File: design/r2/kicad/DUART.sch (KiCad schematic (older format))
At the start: 15 parts, among them IC1 XR68C681CJTR-F, J2 UART_A, J3 UART_B, J4 Conn_01x06, Q1 Crystal

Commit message: Complete schematic capture for r2
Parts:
- removed C11, C12: 100nF, rosco_m68k:C2.5-3, symbol Device:C
- removed C13, C14: 220uF, Capacitor_THT:CP_Radial_D6.3mm_P2.50mm, symbol Device:CP
- removed JP1-5: Conn_02x05_Odd_Even, Connector_PinHeader_2.54mm:PinHeader_2x05_P2.54mm_Vertical, symbol Connector_Generic:Conn_02x05_Odd_Even
- added JP1, JP2: Jumper, Connector_PinHeader_2.54mm:PinHeader_1x02_P2.54mm_Vertical, symbol Device:Jumper
- renumbered C3 to C1, C5 to C2, C8 to C28, C9 to C29, C10 to C30, IC1 to IC4, J2 to J1, J3 to J2
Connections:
- net labels added: IPL2, RW
- net labels removed: IPL3, RnW
- wire segments 50 -> 32
- no-connect marks 6 -> 4
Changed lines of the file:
@@
 $Descr A4 11693 8268
 encoding utf-8
-Sheet 5 5
+Sheet 4 7
 Title "ROSCO_M68K GENERAL PURPOSE MC68010 COMPUTER"
 Date "2021-10-08"
@@
 $EndComp
 $Comp
-L Device:C C3
+L Device:C C1
 U 1 1 5EDD83D0
 P 7550 3850
-F 0 "C3" H 7665 3896 50  0000 L CNN
+F 0 "C1" H 7665 3896 50  0000 L CNN
 F 1 "7pF" H 7665 3805 50  0000 L CNN
 F 2 "Capacitor_THT:C_Rect_L7.0mm_W2.0mm_P5.00mm" H 7588 3700 50  0001 C CNN
@@
 $EndComp
 $Comp
-L Device:C C5
+L Device:C C2
 U 1 1 5EDD8A07
 P 8200 3850
-F 0 "C5" H 8315 3896 50  0000 L CNN
+F 0 "C2" H 8315 3896 50  0000 L CNN
 F 1 "7pF" H 8315 3805 50  0000 L CNN
 F 2 "Capacitor_THT:C_Rect_L7.0mm_W2.0mm_P5.00mm" H 8238 3700 50  0001 C CNN
@@
 D7
 Text GLabel 4400 2600 0    50   Input ~ 0
-RnW
+RW
 Text GLabel 6400 2400 2    50   Input ~ 0
 RESET
@@
 A4
 $Comp
-L Connector:Conn_01x06_Male J2
+L Connector:Conn_01x06_Male J1
 U 1 1 5EE19F70
 P 1250 5850
-F 0 "J2" H 1358 6231 50  0000 C CNN
+F 0 "J1" H 1358 6231 50  0000 C CNN
 F 1 "UART_A" H 1358 6140 50  0000 C CNN
 F 2 "Connector_PinHeader_2.54mm:PinHeader_1x06_P2.54mm_Vertical" H 1250 5850 50  0001 C CNN
@@
 $EndComp
 $Comp
-L Connector:Conn_01x06_Male J3
+L Connector:Conn_01x06_Male J2
 U 1 1 5EE1B2ED
 P 1250 6700
-F 0 "J3" H 1358 7081 50  0000 C CNN
+F 0 "J2" H 1358 7081 50  0000 C CNN
 F 1 "UART_B" H 1358 6990 50  0000 C CNN
 F 2 "Connector_PinHeader_2.54mm:PinHeader_1x06_P2.54mm_Vertical" H 1250 6700 50  0001 C CNN
@@
 Text GLabel 1450 5950 2    50   Output ~ 0
 RXDA
-NoConn ~ 1450 6150
-Text GLabel 10550 5350 2    50   UnSpc ~ 0
+Text GLabel 10650 5200 2    50   UnSpc ~ 0
 VCC
-Text GLabel 8750 5450 0    50   UnSpc ~ 0
+Text GLabel 9500 5200 0    50   UnSpc ~ 0
 VCCUA
-Text GLabel 8750 5350 0    50   UnSpc ~ 0
+Text GLabel 9500 5650 0    50   UnSpc ~ 0
 VCCUB
 Text GLabel 1450 5850 2    50   UnSpc ~ 0
@@
 Text GLabel 1450 6800 2    50   Output ~ 0
 RXDB
-NoConn ~ 1450 7000
 Text GLabel 6400 3100 2    50   Output ~ 0
 SPICS
@@
 TXDA
 $Comp
-L Device:C C8
+L Device:C C28
 U 1 1 5EF9C0B2
 P 1250 1450
-F 0 "C8" V 998 1450 50  0000 C CNN
+F 0 "C28" V 998 1450 50  0000 C CNN
 F 1 "100nF" V 1089 1450 50  0000 C CNN
 F 2 "rosco_m68k:C2.5-3" H 1288 1300 50  0001 C CNN
@@
 $EndComp
 $Comp
-L Device:C C9
+L Device:C C29
 U 1 1 5EF9CBDA
 P 1250 1900
-F 0 "C9" V 998 1900 50  0000 C CNN
+F 0 "C29" V 998 1900 50  0000 C CNN
 F 1 "100nF" V 1089 1900 50  0000 C CNN
 F 2 "rosco_m68k:C2.5-3" H 1288 1750 50  0001 C CNN
@@
 	0    1    1    0
 $EndComp
-$Comp
-L Device:CP C13
-U 1 1 5EF9DA6F
-P 1250 3800
-F 0 "C13" V 1505 3800 50  0000 C CNN
-F 1 "220uF" V 1414 3800 50  0000 C CNN
-F 2 "Capacitor_THT:CP_Radial_D6.3mm_P2.50mm" H 1288 3650 50  0001 C CNN
-F 3 "~" H 1250 3800 50  0001 C CNN
-	1    1250 3800
-	0    -1   -1   0
-$EndComp
-$Comp
-L Device:CP C14
-U 1 1 5EF9E65A
-P 1250 4250
-F 0 "C14" V 1505 4250 50  0000 C CNN
-F 1 "220uF" V 1414 4250 50  0000 C CNN
-F 2 "Capacitor_THT:CP_Radial_D6.3mm_P2.50mm" H 1288 4100 50  0001 C CNN
-F 3 "~" H 1250 4250 50  0001 C CNN
-	1    1250 4250
-	0    -1   -1   0
-$EndComp
 Wire Wire Line
 	1000 1100 1000 1450
-Wire Wire Line
-	1000 4250 1100 4250
 Wire Wire Line
 	1500 1450 1500 1900
@@
 	1400 1900 1500 1900
 Connection ~ 1500 1900
-Wire Wire Line
-	1400 3800 1500 3800
-Wire Wire Line
-	1500 3800 1500 4250
-Wire Wire Line
-	1100 3800 1000 3800
-Wire Wire Line
-	1000 3800 1000 4250
-Wire Wire Line
-	1400 4250 1500 4250
-Connection ~ 1500 4250
-Wire Wire Line
-	1500 4250 1500 4500
 Text GLabel 1000 1100 1    50   UnSpc ~ 0
 VCC
-Text GLabel 1500 4500 3    50   UnSpc ~ 0
+Text GLabel 1500 2500 3    50   UnSpc ~ 0
 GND
 Text GLabel 6400 1800 2    50   UnSpc ~ 0
@@
 CTSB
 $Comp
-L Device:C C10
+L Device:C C30
 U 1 1 5EE63A78
 P 1250 2350
-F 0 "C10" V 998 2350 50  0000 C CNN
+F 0 "C30" V 998 2350 50  0000 C CNN
 F 1 "100nF" V 1089 2350 50  0000 C CNN
 F 2 "rosco_m68k:C2.5-3" H 1288 2200 50  0001 C CNN
@@
 	0    1    1    0
 $EndComp
-$Comp
-L Device:C C11
-U 1 1 5EE644CC
-P 1250 2800
-F 0 "C11" V 998 2800 50  0000 C CNN
-F 1 "100nF" V 1089 2800 50  0000 C CNN
-F 2 "rosco_m68k:C2.5-3" H 1288 2650 50  0001 C CNN
-F 3 "~" H 1250 2800 50  0001 C CNN
-	1    1250 2800
-	0    1    1    0
-$EndComp
-$Comp
-L Device:C C12
-U 1 1 5EE7105F
-P 1250 3250
-F 0 "C12" V 998 3250 50  0000 C CNN
-F 1 "100nF" V 1089 3250 50  0000 C CNN
-F 2 "rosco_m68k:C2.5-3" H 1288 3100 50  0001 C CNN
-F 3 "~" H 1250 3250 50  0001 C CNN
-	1    1250 3250
-	0    1    1    0
-$EndComp
 Wire Wire Line
 	1000 1900 1000 2350
-Connection ~ 1000 3800
 Wire Wire Line
 	1500 1900 1500 2350
-Connection ~ 1500 3800
-Wire Wire Line
-	1400 3250 1500 3250
-Connection ~ 1500 3250
-Wire Wire Line
-	1500 3250 1500 3800
-Wire Wire Line
-	1100 3250 1000 3250
-Connection ~ 1000 3250
-Wire Wire Line
-	1000 3250 1000 3800
-Wire Wire Line
-	1100 2800 1000 2800
-Connection ~ 1000 2800
-Wire Wire Line
-	1000 2800 1000 3250
-Wire Wire Line
-	1400 2800 1500 2800
-Connection ~ 1500 2800
-Wire Wire Line
-	1500 2800 1500 3250
 Wire Wire Line
 	1400 2350 1500 2350
-Connection ~ 1500 2350
-Wire Wire Line
-	1500 2350 1500 2800
 Wire Wire Line
 	1100 2350 1000 2350
-Connection ~ 1000 2350
-Wire Wire Line
-	1000 2350 1000 2800
-$Comp
-L rosco_m68k-rescue:XR68C681CJTR-F-XR68C681 IC1
+$Comp
+L rosco_m68k-rescue:XR68C681CJTR-F-XR68C681 IC4
 U 1 1 603DDDD7
 P 4400 1800
-F 0 "IC1" H 5400 2293 60  0000 C CNN
+F 0 "IC4" H 5400 2293 60  0000 C CNN
 F 1 "XR68C681CJTR-F" H 5400 2187 60  0000 C CNN
 F 2 "Package_LCC:PLCC-44_THT-Socket" H 5400 2040 60  0001 C CNN
@@
 Wire Wire Line
 	8200 2500 6400 2500
-$Comp
-L Connector_Generic:Conn_02x05_Odd_Even JP1-5
-U 1 1 60587A30
-P 9750 5450
-F 0 "JP1-5" H 9800 5867 50  0000 C CNN
-F 1 "Conn_02x05_Odd_Even" H 9800 5776 50  0000 C CNN
-F 2 "Connector_PinHeader_2.54mm:PinHeader_2x05_P2.54mm_Vertical" H 9750 5450 50  0001 C CNN
-F 3 "~" H 9750 5450 50  0001 C CNN
-	1    9750 5450
-	1    0    0    -1
-$EndComp
-Wire Wire Line
-	10550 5350 10300 5350
-Wire Wire Line
-	10050 5450 10300 5450
-Wire Wire Line
-	10300 5450 10300 5350
-Connection ~ 10300 5350
-Wire Wire Line
-	10300 5350 10050 5350
-Wire Wire Line
-	8750 5450 9550 5450
-Wire Wire Line
-	9550 5350 8750 5350
-Wire Wire Line
-	10050 5650 10550 5650
-Wire Wire Line
-	10050 5550 10550 5550
 Text GLabel 6400 3800 2    50   3State ~ 0
-IPL3
+IPL2
 NoConn ~ 4400 3200
 NoConn ~ 4400 3300
@@
 P 3200 6450
 AR Path="/5E53BC83/61644BCE" Ref="#PWR?"  Part="1"
-AR Path="/61622E90/61644BCE" Ref="#PWR?"  Part="1"
-F 0 "#PWR?" H 3200 6300 50  0001 C CNN
+AR Path="/61622E90/61644BCE" Ref="#PWR0101"  Part="1"
+F 0 "#PWR0101" H 3200 6300 50  0001 C CNN
 F 1 "VCC" H 3217 6623 50  0000 C CNN
 F 2 "" H 3200 6450 50  0001 C CNN
@@
 P 3200 6750
 AR Path="/5E53BC83/61644BD4" Ref="#PWR?"  Part="1"
-AR Path="/61622E90/61644BD4" Ref="#PWR?"  Part="1"
-F 0 "#PWR?" H 3200 6500 50  0001 C CNN
+AR Path="/61622E90/61644BD4" Ref="#PWR0102"  Part="1"
+F 0 "#PWR0102" H 3200 6500 50  0001 C CNN
 F 1 "GND" H 3205 6577 50  0000 C CNN
 F 2 "" H 3200 6750 50  0001 C CNN
@@
 Wire Wire Line
 	3200 6650 3200 6750
+Wire Wire Line
+	1500 2350 1500 2500
+Connection ~ 1500 2350
+$Comp
+L Device:Jumper JP2
+U 1 1 616FCABD
+P 10000 5650
+F 0 "JP2" H 10000 5914 50  0000 C CNN
+F 1 "Jumper" H 10000 5823 50  0000 C CNN
+F 2 "Connector_PinHeader_2.54mm:PinHeader_1x02_P2.54mm_Vertical" H 10000 5650 50  0001 C CNN
+F 3 "~" H 10000 5650 50  0001 C CNN
+	1    10000 5650
+	1    0    0    -1
+$EndComp
+$Comp
+L Device:Jumper JP1
+U 1 1 616FD293
+P 10000 5200
+F 0 "JP1" H 10000 5464 50  0000 C CNN
+F 1 "Jumper" H 10000 5373 50  0000 C CNN
+F 2 "Connector_PinHeader_2.54mm:PinHeader_1x02_P2.54mm_Vertical" H 10000 5200 50  0001 C CNN
+F 3 "~" H 10000 5200 50  0001 C CNN
+	1    10000 5200
+	1    0    0    -1
+$EndComp
+Wire Wire Line
+	9500 5200 9700 5200
+Wire Wire Line
+	10300 5200 10500 5200
+Wire Wire Line
+	10300 5650 10500 5650
+Wire Wire Line
+	10500 5650 10500 5200
+Connection ~ 10500 5200
+Wire Wire Line
+	10500 5200 10650 5200
+Wire Wire Line
+	9500 5650 9700 5650
+Text GLabel 1450 6150 2    50   Input ~ 0
+RTSA
+Text GLabel 1450 7000 2    50   Input ~ 0
+RTSB
 $EndSCHEMATC

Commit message: Tidy up footprints
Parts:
- added LED1: GREEN, rosco_m68k:LED5MM, symbol rosco_m68k-eagle-import:LED5MM
- added LED2: RED, rosco_m68k:LED5MM, symbol rosco_m68k-eagle-import:LED5MM
- added R10, R11: 330R, rosco_m68k:0207_10, symbol rosco_m68k-eagle-import:R-EU_0207_10
- C1, C2: footprint Capacitor_THT:C_Rect_L7.0mm_W2.0mm_P5.00mm -> rosco_m68k:C2.5-3
- J1, J2: footprint Connector_PinHeader_2.54mm:PinHeader_1x06_P2.54mm_Vertical -> rosco_m68k:1X06
- JP1, JP2: footprint Connector_PinHeader_2.54mm:PinHeader_1x02_P2.54mm_Vertical -> rosco_m68k:1X02
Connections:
- wire segments 32 -> 41
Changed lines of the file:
@@
 $Descr A4 11693 8268
 encoding utf-8
-Sheet 4 7
+Sheet 3 7
 Title "ROSCO_M68K GENERAL PURPOSE MC68010 COMPUTER"
 Date "2021-10-08"
@@
 F 0 "C1" H 7665 3896 50  0000 L CNN
 F 1 "7pF" H 7665 3805 50  0000 L CNN
-F 2 "Capacitor_THT:C_Rect_L7.0mm_W2.0mm_P5.00mm" H 7588 3700 50  0001 C CNN
+F 2 "rosco_m68k:C2.5-3" H 7588 3700 50  0001 C CNN
 F 3 "~" H 7550 3850 50  0001 C CNN
 	1    7550 3850
@@
 F 0 "C2" H 8315 3896 50  0000 L CNN
 F 1 "7pF" H 8315 3805 50  0000 L CNN
-F 2 "Capacitor_THT:C_Rect_L7.0mm_W2.0mm_P5.00mm" H 8238 3700 50  0001 C CNN
+F 2 "rosco_m68k:C2.5-3" H 8238 3700 50  0001 C CNN
 F 3 "~" H 8200 3850 50  0001 C CNN
 	1    8200 3850
@@
 F 0 "J1" H 1358 6231 50  0000 C CNN
 F 1 "UART_A" H 1358 6140 50  0000 C CNN
-F 2 "Connector_PinHeader_2.54mm:PinHeader_1x06_P2.54mm_Vertical" H 1250 5850 50  0001 C CNN
+F 2 "rosco_m68k:1X06" H 1250 5850 50  0001 C CNN
 F 3 "~" H 1250 5850 50  0001 C CNN
 	1    1250 5850
@@
 F 0 "J2" H 1358 7081 50  0000 C CNN
 F 1 "UART_B" H 1358 6990 50  0000 C CNN
-F 2 "Connector_PinHeader_2.54mm:PinHeader_1x06_P2.54mm_Vertical" H 1250 6700 50  0001 C CNN
+F 2 "rosco_m68k:1X06" H 1250 6700 50  0001 C CNN
 F 3 "~" H 1250 6700 50  0001 C CNN
 	1    1250 6700
@@
 NoConn ~ 4400 3300
 NoConn ~ 4400 3400
-Text GLabel 6400 1900 2    50   UnSpc ~ 0
-GND
-Text GLabel 6400 2000 2    50   UnSpc ~ 0
-GND
 Text GLabel 4400 2000 0    50   UnSpc ~ 0
 GND
@@
 F 0 "JP2" H 10000 5914 50  0000 C CNN
 F 1 "Jumper" H 10000 5823 50  0000 C CNN
-F 2 "Connector_PinHeader_2.54mm:PinHeader_1x02_P2.54mm_Vertical" H 10000 5650 50  0001 C CNN
+F 2 "rosco_m68k:1X02" H 10000 5650 50  0001 C CNN
 F 3 "~" H 10000 5650 50  0001 C CNN
 	1    10000 5650
@@
 F 0 "JP1" H 10000 5464 50  0000 C CNN
 F 1 "Jumper" H 10000 5373 50  0000 C CNN
-F 2 "Connector_PinHeader_2.54mm:PinHeader_1x02_P2.54mm_Vertical" H 10000 5200 50  0001 C CNN
+F 2 "rosco_m68k:1X02" H 10000 5200 50  0001 C CNN
 F 3 "~" H 10000 5200 50  0001 C CNN
 	1    10000 5200
@@
 Text GLabel 1450 7000 2    50   Input ~ 0
 RTSB
+$Comp
+L rosco_m68k-eagle-import:R-EU_0207_10 R?
+U 1 1 6161B40D
+P 6850 1300
+AR Path="/6161B40D" Ref="R?"  Part="1"
+AR Path="/5E53B952/6161B40D" Ref="R?"  Part="1"
+AR Path="/60FBFA5C/6161B40D" Ref="R?"  Part="1"
+AR Path="/61043B8D/6161B40D" Ref="R?"  Part="1"
+AR Path="/6162E38E/6161B40D" Ref="R?"  Part="1"
+AR Path="/61622E90/6161B40D" Ref="R10"  Part="1"
+F 0 "R10" V 6991 1350 59  0000 L BNN
+F 1 "330R" V 6880 1350 59  0000 L BNN
+F 2 "rosco_m68k:0207_10" H 6850 1300 50  0001 C CNN
+F 3 "" H 6850 1300 50  0001 C CNN
+	1    6850 1300
+	0    -1   -1   0
+$EndComp
+$Comp
+L rosco_m68k-eagle-import:LED5MM LED?
+U 1 1 6161B413
+P 6850 1600
+AR Path="/6161B413" Ref="LED?"  Part="1"
+AR Path="/5E53B952/6161B413" Ref="LED?"  Part="1"
+AR Path="/60FBFA5C/6161B413" Ref="LED?"  Part="1"
+AR Path="/61043B8D/6161B413" Ref="LED?"  Part="1"
+AR Path="/6162E38E/6161B413" Ref="LED?"  Part="1"
+AR Path="/61622E90/6161B413" Ref="LED1"  Part="1"
+F 0 "LED1" H 7100 1700 59  0000 R TNN
+F 1 "GREEN" H 7200 1600 59  0000 R TNN
+F 2 "rosco_m68k:LED5MM" H 6850 1600 50  0001 C CNN
+F 3 "" H 6850 1600 50  0001 C CNN
+	1    6850 1600
+	1    0    0    -1
+$EndComp
+$Comp
+L rosco_m68k-eagle-import:R-EU_0207_10 R?
+U 1 1 6161C7AA
+P 7350 1300
+AR Path="/6161C7AA" Ref="R?"  Part="1"
+AR Path="/5E53B952/6161C7AA" Ref="R?"  Part="1"
+AR Path="/60FBFA5C/6161C7AA" Ref="R?"  Part="1"
+AR Path="/61043B8D/6161C7AA" Ref="R?"  Part="1"
+AR Path="/6162E38E/6161C7AA" Ref="R?"  Part="1"
+AR Path="/61622E90/6161C7AA" Ref="R11"  Part="1"
+F 0 "R11" V 7491 1350 59  0000 L BNN
+F 1 "330R" V 7380 1350 59  0000 L BNN
+F 2 "rosco_m68k:0207_10" H 7350 1300 50  0001 C CNN
+F 3 "" H 7350 1300 50  0001 C CNN
+	1    7350 1300
+	0    -1   -1   0
+$EndComp
+$Comp
+L rosco_m68k-eagle-import:LED5MM LED?
+U 1 1 6161C7B0
+P 7350 1600
+AR Path="/6161C7B0" Ref="LED?"  Part="1"
+AR Path="/5E53B952/6161C7B0" Ref="LED?"  Part="1"
+AR Path="/60FBFA5C/6161C7B0" Ref="LED?"  Part="1"
+AR Path="/61043B8D/6161C7B0" Ref="LED?"  Part="1"
+AR Path="/6162E38E/6161C7B0" Ref="LED?"  Part="1"
+AR Path="/61622E90/6161C7B0" Ref="LED2"  Part="1"
+F 0 "LED2" H 7600 1700 59  0000 R TNN
+F 1 "RED" H 7700 1600 59  0000 R TNN
+F 2 "rosco_m68k:LED5MM" H 7350 1600 50  0001 C CNN
+F 3 "" H 7350 1600 50  0001 C CNN
+	1    7350 1600
+	1    0    0    -1
+$EndComp
+Wire Wire Line
+	6400 1900 6850 1900
+Wire Wire Line
+	6850 1900 6850 1800
+Wire Wire Line
+	6400 2000 7350 2000
+Wire Wire Line
+	7350 2000 7350 1800
+$Comp
+L power:VCC #PWR04
+U 1 1 6161F2BF
+P 7100 800
+F 0 "#PWR04" H 7100 650 50  0001 C CNN
+F 1 "VCC" H 7117 973 50  0000 C CNN
+F 2 "" H 7100 800 50  0001 C CNN
+F 3 "" H 7100 800 50  0001 C CNN
+	1    7100 800
+	1    0    0    -1
+$EndComp
+Wire Wire Line
+	6850 1100 6850 950
+Wire Wire Line
+	6850 950  7100 950
+Wire Wire Line
+	7100 950  7100 800
+Wire Wire Line
+	7350 1100 7350 950
+Wire Wire Line
+	7350 950  7100 950
+Connection ~ 7100 950
 $EndSCHEMATC

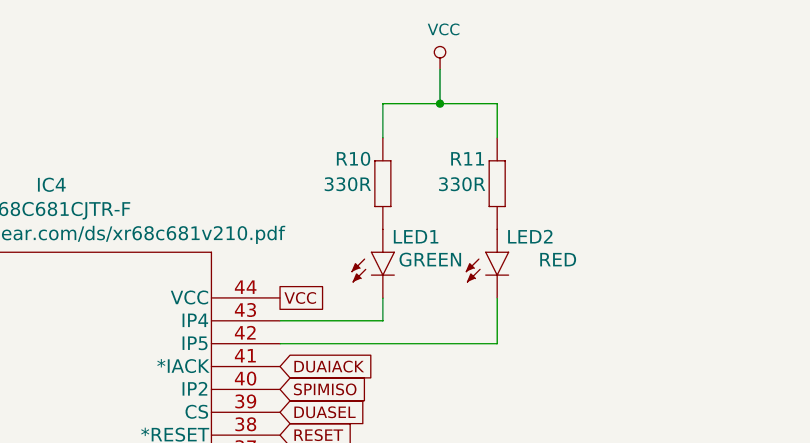
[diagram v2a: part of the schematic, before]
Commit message: Schematic / GAL tweaks and do layout
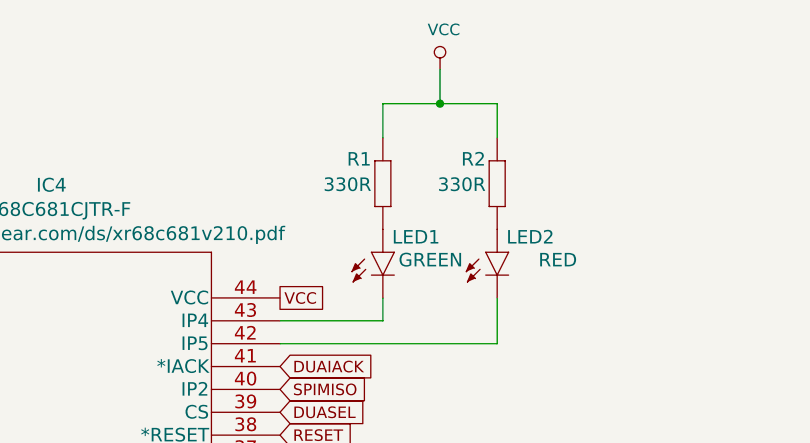
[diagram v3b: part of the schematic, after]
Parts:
- renumbered R10 to R1, R11 to R2
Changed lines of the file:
@@
 AR Path="/61043B8D/6161B40D" Ref="R?"  Part="1"
 AR Path="/6162E38E/6161B40D" Ref="R?"  Part="1"
-AR Path="/61622E90/6161B40D" Ref="R10"  Part="1"
-F 0 "R10" V 6991 1350 59  0000 L BNN
+AR Path="/61622E90/6161B40D" Ref="R1"  Part="1"
+F 0 "R1" V 6991 1350 59  0000 L BNN
 F 1 "330R" V 6880 1350 59  0000 L BNN
 F 2 "rosco_m68k:0207_10" H 6850 1300 50  0001 C CNN
@@
 AR Path="/61043B8D/6161C7AA" Ref="R?"  Part="1"
 AR Path="/6162E38E/6161C7AA" Ref="R?"  Part="1"
-AR Path="/61622E90/6161C7AA" Ref="R11"  Part="1"
-F 0 "R11" V 7491 1350 59  0000 L BNN
+AR Path="/61622E90/6161C7AA" Ref="R2"  Part="1"
+F 0 "R2" V 7491 1350 59  0000 L BNN
 F 1 "330R" V 7380 1350 59  0000 L BNN
 F 2 "rosco_m68k:0207_10" H 7350 1300 50  0001 C CNN
